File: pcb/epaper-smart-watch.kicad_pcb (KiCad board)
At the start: 2 copper layers, 29.2 x 29.2 mm, 66 parts, among them J1 AXT624124, J3 Lithium Battery 3.7V, M1 Motor_DC, P1 USB_C_Plug_USB2.0, Q1 MMBT3904, Q3 Si1308EDL, SW1 BTN, SW2 BTN, SW3 BTN, SW4 BTN, U1 CH340E, U2 STM32WB1MMCH6TR, U3 LSM6DS3

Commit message: V2 soon...
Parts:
- removed the C20 at (154.6, 100.1)
- removed the C21 at (156.5, 100.1)
- removed the C9 at (147.3, 94.3)
- removed the D1 at (138.0, 93.8)
- removed the D3 at (138.0, 96.7)
- removed the D4 at (138.0, 99.6)
- removed JP3: SolderJumper_3_Bridged12, Jumper:SolderJumper-3_P1.3mm_Bridged12_RoundedPad1.0x1.5mm_NumberLabels
- removed PS1: STNS01PUR, SamacSys:SON45P300X300X80-13N-D
- removed Q1: MMBT3904, Package_TO_SOT_SMD:SOT-23
- removed the R2 at (147.4, 98.3)
- removed the R9 at (136.8, 105.6)
- added AC1: BMA400, Package_LGA:LGA-12_2x2mm_P0.5mm, F.Cu at (225.1, 99.8)
- added BZ1: Buzzer, Jumper:SolderJumper-2_P1.3mm_Open_Pad1.0x1.5mm, B.Cu at (141.9, 107.2)
- added C10: 0.1uF, Capacitor_SMD:C_0402_1005Metric, F.Cu at (212.6, 103.7)
- added C22: 10uF, Capacitor_SMD:C_0603_1608Metric, F.Cu at (194.9, 87.4)
- added C5: 100nF, Capacitor_SMD:C_0402_1005Metric, F.Cu at (213.2, 98.0)
- added C6: 100nF, Capacitor_SMD:C_0402_1005Metric, F.Cu at (213.3, 95.1)
- added D2: LED, LED_SMD:LED_0603_1608Metric, F.Cu at (210.9, 100.0)
- added D6: MBR0530, Diode_SMD:D_SOD-123, F.Cu at (198.2, 90.3)
- added IC2: NPM1100-QDAA-R7, SamasSys:QFN50P400X400X90-25N-D, F.Cu at (141.6, 75.1)
- added IC3: MAX17048G+T10, SamasSys:SON50P200X200X80-9N-D, F.Cu at (214.8, 101.5)
- added IC4: AP3032, SamasSys:SOT95P280X145-6N, F.Cu at (130.1, 84.0)
- added J10: ~, TestPoint:TestPoint_Pad_D1.0mm, B.Cu at (170.4, 85.0)
- added J11: ~, TestPoint:TestPoint_Pad_D1.0mm, B.Cu at (170.4, 88.1)
- added J12: ~, TestPoint:TestPoint_Pad_D1.0mm, B.Cu at (170.4, 91.2)
- added J13: ~, TestPoint:TestPoint_Pad_D1.0mm, B.Cu at (173.5, 85.0)
- added J14: ~, TestPoint:TestPoint_Pad_D1.0mm, B.Cu at (173.5, 88.1)
- added J15: ~, TestPoint:TestPoint_Pad_D1.0mm, B.Cu at (173.5, 91.2)
- added J16: Touch3, TestPoint:TestPoint_Pad_D1.0mm, B.Cu at (163.3, 86.5)
- added J17: Touch2, TestPoint:TestPoint_Pad_D1.0mm, B.Cu at (163.3, 89.6)
- added J18: Touch1, TestPoint:TestPoint_Pad_D1.0mm, B.Cu at (163.3, 92.7)
- added J4: ~, TestPoint:TestPoint_Pad_D1.0mm, B.Cu at (162.7, 82.5)
- added J7: ~, TestPoint:TestPoint_Pad_D1.0mm, B.Cu at (167.4, 85.0)
- added J8: ~, TestPoint:TestPoint_Pad_D1.0mm, B.Cu at (167.4, 88.1)
- added J9: ~, TestPoint:TestPoint_Pad_D1.0mm, B.Cu at (167.4, 91.2)
- added L1: 2.2uH, Inductor_SMD:L_0603_1608Metric, F.Cu at (202.5, 99.6)
- added L3: 6.8uH, Inductor_SMD:L_0603_1608Metric, F.Cu at (200.2, 87.6)
- added Q3: AO3400A, Package_TO_SOT_SMD:SOT-23, F.Cu at (224.7, 95.8)
- added R1: 10k, Resistor_SMD:R_0402_1005Metric, F.Cu at (212.2, 96.7)
- added R1: 10k, Resistor_SMD:R_0402_1005Metric, F.Cu at (210.0, 91.5)
- added R10: 750k, Resistor_SMD:R_0402_1005Metric, F.Cu at (199.9, 82.4)
- added R11: 100k, Resistor_SMD:R_0402_1005Metric, F.Cu at (198.2, 84.3)
- added R13: 1k, Resistor_SMD:R_0402_1005Metric, F.Cu at (212.9, 101.1)
- added R2: 10k, Resistor_SMD:R_0402_1005Metric, F.Cu at (208.6, 93.7)
- added R2: 10k, Resistor_SMD:R_0402_1005Metric, F.Cu at (209.6, 93.7)
- added R5: 8.2k, Resistor_SMD:R_0402_1005Metric, F.Cu at (210.7, 97.0)
- added R8: 100k, Resistor_SMD:R_0402_1005Metric, F.Cu at (214.6, 93.0)
- added SW6: SW_Push, Button_Switch_SMD:SW_SPST_TS-1088-xR020, F.Cu at (158.4, 74.5)
- added U4: XT25F32FDTIGT, ProjectLibrary:DFN-8_L3.0-W2.0-P0.50-BL-EP_XT25XXX, F.Cu at (148.2, 75.1)
- C11: renamed from C13; value 2.2uF -> 100nF
- C13: renamed from C1; footprint Capacitor_SMD:C_0402_1005Metric -> Capacitor_SMD:C_0603_1608Metric
- C16: value 4.7uF -> 1uF; footprint Capacitor_SMD:C_0402_1005Metric -> Capacitor_SMD:C_0603_1608Metric
- C19: value 2.7pF -> 1uF/16V
- C2: renamed from C17; value 0.1uF -> 10uF; footprint Capacitor_SMD:C_0402_1005Metric -> Capacitor_SMD:C_0603_1608Metric
- C21: renamed from C4; footprint Capacitor_SMD:C_0402_1005Metric -> Capacitor_SMD:C_0603_1608Metric
- C22: value 2.2uF -> 3.3pF
- C24, C25: value 0.1uF -> 100nF
- C3: renamed from C18; footprint Capacitor_SMD:C_0402_1005Metric -> Capacitor_SMD:C_0603_1608Metric
- C4: renamed from C15; value 0.1uF -> 10uF; footprint Capacitor_SMD:C_0402_1005Metric -> Capacitor_SMD:C_0603_1608Metric
- C7: renamed from C14; value 1uF -> 2.2uF
- C8: renamed from C12; value 4.7uF -> 1uF
- J5: renamed from J3; moved to B.Cu
- J6: renamed from J1; footprint FPC:AXT624124 -> ProjectLibrary:AXT624124
- M1: moved to B.Cu
- P1: footprint USBC:USB-C-SMD_KH-TYPE-C-16P -> ProjectLibrary:USB-C-SMD_TYPE-C-16P-CB0.8-073
- Q2: renamed from Q3; footprint Package_TO_SOT_SMD:SOT-323_SC-70 -> Package_TO_SOT_SMD:SOT-23
- R12: renamed from R1; value 2k -> 100k
- R14: value 1k -> 100k
- R15: value 1k -> 10
- R16: value 1k -> 10k
- R6: renamed from R5; value 600 -> 1k
- R7: value 10K -> 100
- U1: value CH340E -> BME280; footprint Package_SO:MSOP-10_3x3mm_P0.5mm -> Package_LGA:Bosch_LGA-8_2.5x2.5mm_P0.65mm_ClockwisePinNumbering
- U2: value STM32WB1MMCH6TR -> USBLC6-2SC6; footprint EasyEda2Kicad:LGA-77_L10.0-W6.5-STM32WB1MMCH6TR -> Package_TO_SOT_SMD:SOT-23-6
- U3: value LSM6DS3 -> STM32WB5MMG; footprint Package_LGA:LGA-14_3x2.5mm_P0.5mm_LayoutBorder3x4y -> RF_Module:ST-SiP-LGA-86-11x7.3mm
- moved D3 73.3 mm to (210.9, 98.5), turned to 180 degrees
- moved C9 73.0 mm to (218.5, 89.0)
- moved U1 72.8 mm to (213.5, 91.1)
- moved D4 72.1 mm to (216.6, 91.2), turned to 90 degrees
- moved R3 71.6 mm to (207.5, 101.7)
- moved R16 71.6 mm to (215.5, 98.7), turned to 90 degrees
- moved D1 69.3 mm to (210.9, 101.5), turned to 0 degrees
- moved R14 69.0 mm to (211.0, 84.4)
- moved C2 68.6 mm to (207.7, 99.7)
- moved C22 68.0 mm to (209.6, 80.7), turned to 90 degrees
- moved C11 67.9 mm to (210.7, 95.8), turned to 180 degrees
- moved C8 67.8 mm to (208.9, 91.6), turned to 90 degrees
- moved C25 67.6 mm to (209.8, 84.7), turned to 90 degrees
- moved C4 67.5 mm to (208.9, 96.2)
- moved C24 67.2 mm to (209.7, 88.8)
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- renumbered C2 to C12, C8 to C14, C3 to C15, C11 to C17, C7 to C18, C6 to C19, C5 to C20, C10 to C23, C23 to C9, D6 to D1, D2 to D3, D9 to D4, D7 to D5, D5 to D7, L1 to L2, R6 to R9, SW1 to SW2, SW2 to SW3, SW3 to SW4, SW4 to SW5
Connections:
- net /RESR renamed /EPD_RESR
- net /VCOM renamed /EPD_VCOM
- net /VGH renamed /EPD_VGH
- net /VGL renamed /EPD_VGL
- C11 pad 1: /VBUS -> +3V0
- C12 pad 1: /EPD_VDD -> +3V0
- C13 pad 1: /EPD_VDD -> +3V0
- C16 pad 1: /EPD_VDD -> /EPD_LIGHT_PWR_POS
- C16 pad 2: GND -> /EPD_LIGHT_PWR_NEG
- C19 pad 1: Net-(U2-PB1) -> Net-(J6-Pin_5)
- C19 pad 1: Net-(J1-Pin_5) -> Net-(J6-Pin_5)
- C2 pad 1: Net-(U1-V3) -> +3V0
- C24 pad 1: /EPD_VDD -> GND
- C24 pad 2: GND -> /NRST
- C25 pad 1: /EPD_VDD -> GND
- C25 pad 2: GND -> Net-(U3-PC13)
- C3 pad 1: Net-(U1-~{RTS}) -> Net-(IC2-DEC)
- C3 pad 2: /NRST -> GND
- C4 pad 1: /VBUS -> /VSYS
- C7 pad 1: /EPD_VDD -> +5V
- C9 pad 1: Net-(D9-K) -> +3V0
- C9 pad 2: GND -> Net-(D4-A)
- D1 pad 1: GND -> Net-(D1-K)
- D1 pad 2: Net-(D6-A) -> /VSYS
- D3 pad 1: /CHG -> GND
- D4 pad 1: Net-(D9-K) -> +3V0
- D4 pad 2: GND -> Net-(D4-A)
- J5 pad 2: GND -> Net-(J5-Pin_2)
- J5 pad 3: Net-(J3-Pin_3) -> GND
- J6 pad 12: /CSB -> /EPD_CSB
- J6 pad 13: /DC -> /EPD_DC
- J6 pad 14: /RST_N -> /EPD_RST_N
- J6 pad 15: /BUSY -> /EPD_BUSY
- J6 pad 16: Net-(J1-Pin_16) -> Net-(J6-Pin_16)
- J6 pad 21: /GDR -> /EPD_GDR
- J6 pad 23: /FL+ -> /EPD_LIGHT_PWR_POS
- J6 pad 24: /FL- -> /EPD_LIGHT_PWR_NEG
- J6 pad 5: Net-(J1-Pin_5) -> Net-(J6-Pin_5)
- J6 pad 9: /EPD_VDD -> +3V0
- JP1 pad 1: Net-(JP1-A) -> Net-(J6-Pin_16)
- JP1 pad 2: /TXD -> GND
- JP1 pad 3: Net-(JP1-B) -> +3V0
- JP2 pad 1: Net-(JP1-B) -> Net-(JP2-A)
- JP2 pad 2: /RXD -> Net-(IC2-NTC)
- JP2 pad 3: Net-(JP1-A) -> Net-(J5-Pin_2)
- L2 pad 1: /EPD_VDD -> +3V0
- M1 pad 1: Net-(D9-K) -> +3V0
- M1 pad 2: GND -> Net-(D4-A)
- P1 pad A6: /D+ -> Net-(P1-D+-PadA6)
- P1 pad A7: /D- -> Net-(P1-D--PadA7)
- P1 pad A8: unconnected-(P1-SBU1-PadA8) -> (no net)
- P1 pad B6: /D+ -> Net-(P1-D+-PadA6)
- P1 pad B7: /D- -> Net-(P1-D--PadA7)
- P1 pad B8: unconnected-(P1-SBU2-PadB8) -> (no net)
- Q2 pad 1: /GDR -> /EPD_GDR
- R12 pad 1: Net-(PS1-ISET) -> GND
- R12 pad 2: Net-(R1-Pad2) -> /EPD_GDR
- R14 pad 1: Net-(U1-TNOW) -> +3V0
- R14 pad 2: Net-(D6-A) -> /FLASH_CS
- R15 pad 1: Net-(U1-TXD) -> GND
- R15 pad 2: Net-(JP1-A) -> /EPD_LIGHT_PWR_NEG
- R16 pad 1: Net-(U1-RXD) -> Net-(JP2-A)
- R16 pad 2: Net-(JP1-B) -> GND
- R6 pad 1: /EPD_VDD -> +5V
- R7 pad 1: /EPD_VDD -> Net-(Q3-G)
- R7 pad 2: /Accel_SDA -> /VIB
- SWD1 pad 6: /EPD_VDD -> +3V0
- U1 pad 1: /D+ -> GND
- U1 pad 2: /D- -> Net-(U1-CSB)
- U1 pad 3: GND -> /ACCL_SDA
- U1 pad 4: Net-(U1-~{RTS}) -> /ACCL_SCL
- U1 pad 5: unconnected-(U1-~{CTS}-Pad5) -> GND
- U1 pad 6: Net-(U1-TNOW) -> +3V0
- U1 pad 7: /VBUS -> GND
- U1 pad 8: Net-(U1-TXD) -> +3V0
- U2 pad 1: GND -> Net-(P1-D--PadA7)
- U2 pad 3: GND -> Net-(P1-D+-PadA6)
- U2 pad 4: GND -> /D+
- U2 pad 5: GND -> +5V
- U2 pad 6: Net-(U2-ANT_IN) -> /D-
- U3 pad 1: unconnected-(U3-SDO/SA0-Pad1) -> /EPD_BUSY
- U3 pad 10: unconnected-(U3-NC-Pad10) -> /NRST
- U3 pad 11: unconnected-(U3-NC-Pad11) -> /ACCL_SDA
- U3 pad 12: /Accel_CS -> /ACCL_INT1
- U3 pad 13: /Accel_SCL -> Net-(U3-PH3-BOOT0)
- U3 pad 14: /Accel_SDA -> /ACCL_SCL
- U3 pad 4: /Accel_INT1 -> +3V0
- U3 pad 5: /EPD_VDD -> GND
- U3 pad 6: GND -> +3V0
- U3 pad 7: GND -> unconnected-(U3-PC3-Pad7)
- U3 pad 8: /EPD_VDD -> unconnected-(U3-PC2-Pad8)
- U3 pad 9: unconnected-(U3-INT2-Pad9) -> /ACCL_INT2
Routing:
- net /EPD_VDD: track 71.7 -> 0.00 mm, vias 8 -> 0
- net GND: track 54.7 -> 0.00 mm, vias 17 -> 0
- net /VBUS: track 34.2 -> 0.00 mm, vias 5 -> 0
- net /BTN_1: track 32.7 -> 0.00 mm, vias 2 -> 0
- net /BTN_4: track 24.7 -> 0.00 mm, vias 2 -> 0
- net /RST_N: track 22.1 -> 0.00 mm, vias 2 -> 0
- net /BUSY: track 18.6 -> 0.00 mm, vias 2 -> 0
- net /DC: track 18.4 -> 0.00 mm, vias 2 -> 0
- net /BATMS: track 18.3 -> 0.00 mm, vias 2 -> 0
- net /EPD_SPICL: track 18.1 -> 0.00 mm, vias 2 -> 0
- net /EPD_MOSI: track 17.0 -> 0.00 mm, vias 2 -> 0
- net /CSB: track 15.1 -> 0.00 mm, vias 2 -> 0
- net Net-(D5-A): track 15.0 -> 0.00 mm
- net /NRST: track 14.9 -> 0.00 mm, vias 3 -> 0
- net /RXD: track 11.7 -> 0.00 mm, vias 1 -> 0
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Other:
- board size 29.2 x 29.2 mm -> 41 x 36 mm
- copper layers 2 -> 4

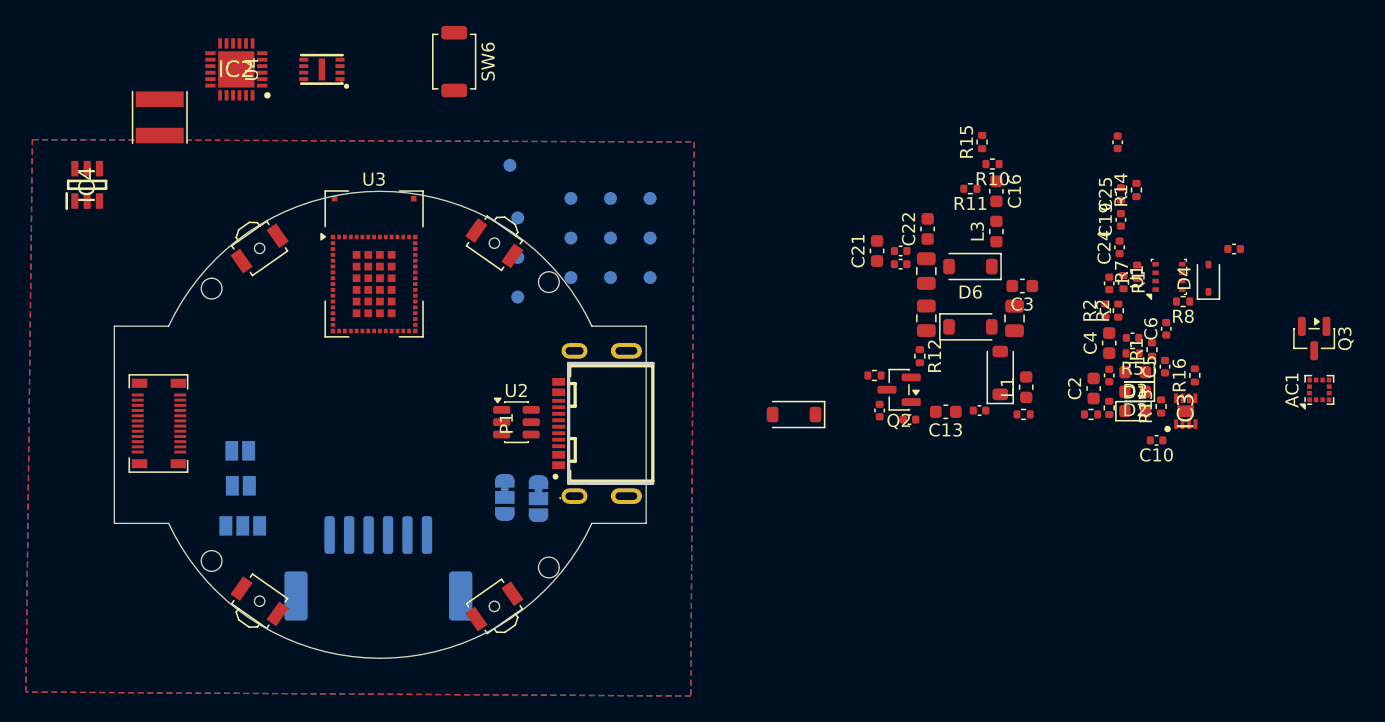
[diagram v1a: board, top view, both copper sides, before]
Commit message: Routed the board, will do verification check soon
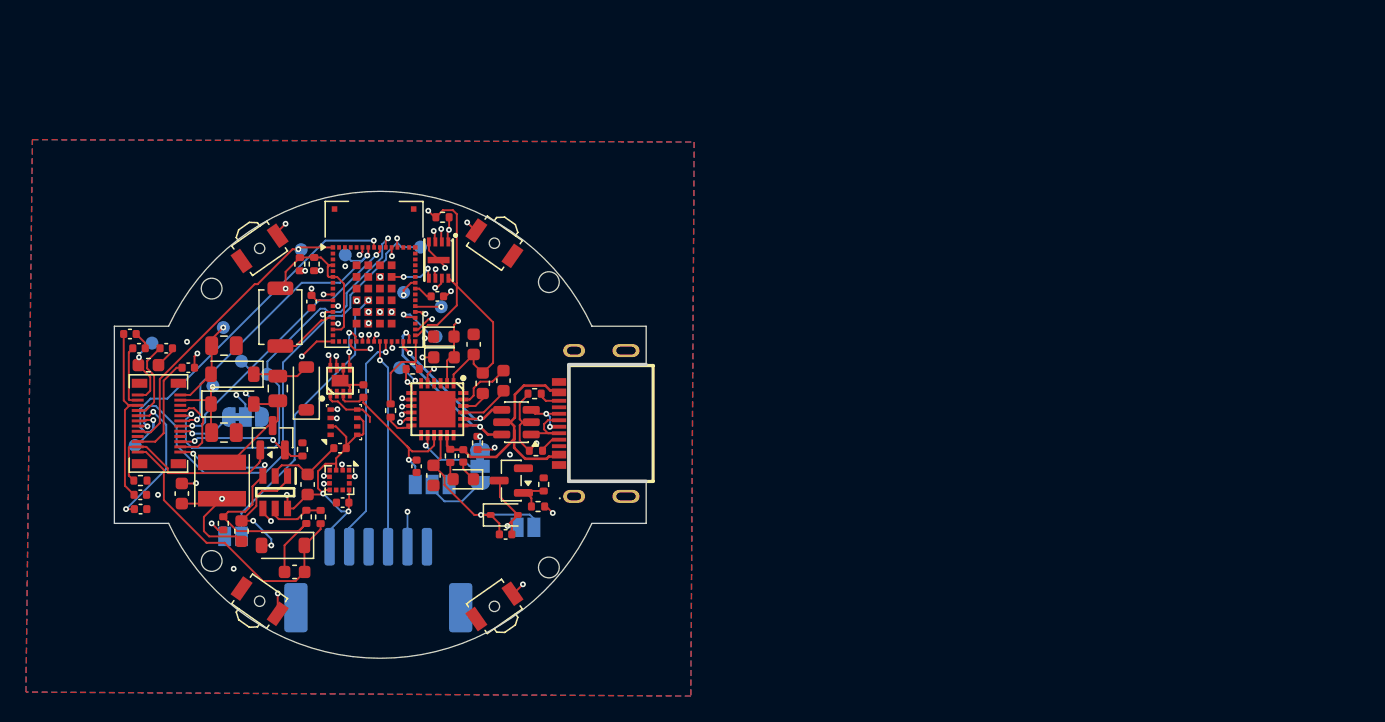
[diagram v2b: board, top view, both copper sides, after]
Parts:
- removed the C22 at (209.6, 80.7)
- removed C5: 100nF, Capacitor_SMD:C_0402_1005Metric
- removed the R1 at (212.2, 96.7)
- removed the R1 at (210.0, 91.5)
- removed the R2 at (208.6, 93.7)
- removed the R2 at (209.6, 93.7)
- added R1: 10k, Resistor_SMD:R_0402_1005Metric, F.Cu at (147.6, 90.1)
- added R2: 10k, Resistor_SMD:R_0402_1005Metric, F.Cu at (146.5, 90.1)
- P1: footprint ProjectLibrary:USB-C-SMD_TYPE-C-16P-CB0.8-073 -> USB-C-SMD_SHOU_TYPE-C-16P-CB1.6
- moved C19 78.5 mm to (134.2, 107.9), turned to 0 degrees
- moved AC1 75.9 mm to (149.6, 106.8), turned to -90 degrees
- moved R15 65.5 mm to (140.6, 110.1)
- moved IC3 65.2 mm to (149.6, 99.1)
- moved C12 65.1 mm to (134.2, 109.0)
- moved U1 64.6 mm to (149.9, 102.3)
- moved C6 64.4 mm to (149.6, 104.3), turned to 0 degrees
- moved Q3 62.9 mm to (162.8, 106.8), turned to 180 degrees
- moved L3 62.6 mm to (142.0, 110.7), turned to -90 degrees
- moved C24 62.4 mm to (147.4, 93.0)
- moved C11 62.2 mm to (149.8, 108.5)
- moved C16 61.6 mm to (146.1, 113.8), turned to 180 degrees
- moved C10 61.3 mm to (151.4, 99.9), turned to 90 degrees
- moved R12 60.9 mm to (134.2, 106.8), turned to 180 degrees
- moved C9 60.3 mm to (162.4, 111.0)
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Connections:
- C9 pad 1: +3V0 -> /VSYS
- D4 pad 1: +3V0 -> /VSYS
- M1 pad 1: +3V0 -> /VSYS
- U1 pad 2: Net-(U1-CSB) -> +3V0
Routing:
- net +3V0: track 0.00 -> 143.6 mm, vias 0 -> 10
- net GND: track 0.00 -> 74.0 mm, vias 0 -> 14
- net /VSYS: track 0.00 -> 41.5 mm, vias 0 -> 3
- net /EPD_DC: track 0.00 -> 40.0 mm, vias 0 -> 2
- net /EPD_MOSI: track 0.00 -> 32.8 mm, vias 0 -> 2
- net /EPD_SPICL: track 0.00 -> 32.4 mm, vias 0 -> 2
- net /BTN_4: track 0.00 -> 26.3 mm, vias 0 -> 2
- net /BTN_1: track 0.00 -> 24.9 mm, vias 0 -> 2
- net /EPD_LIGHT_PWR_NEG: track 0.00 -> 24.8 mm, vias 0 -> 2
- net /NRST: track 0.00 -> 24.7 mm, vias 0 -> 2
- net /EPD_CSB: track 0.00 -> 23.9 mm, vias 0 -> 2
- net /EPD_LIGHT: track 0.00 -> 23.6 mm, vias 0 -> 2
- net /EPD_BUSY: track 0.00 -> 23.0 mm, vias 0 -> 1
- net /EPD_LIGHT_PWR_POS: track 0.00 -> 22.9 mm
- net /VIB: track 0.00 -> 22.7 mm, vias 0 -> 2
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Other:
- outline, holes or cut-outs redrawn

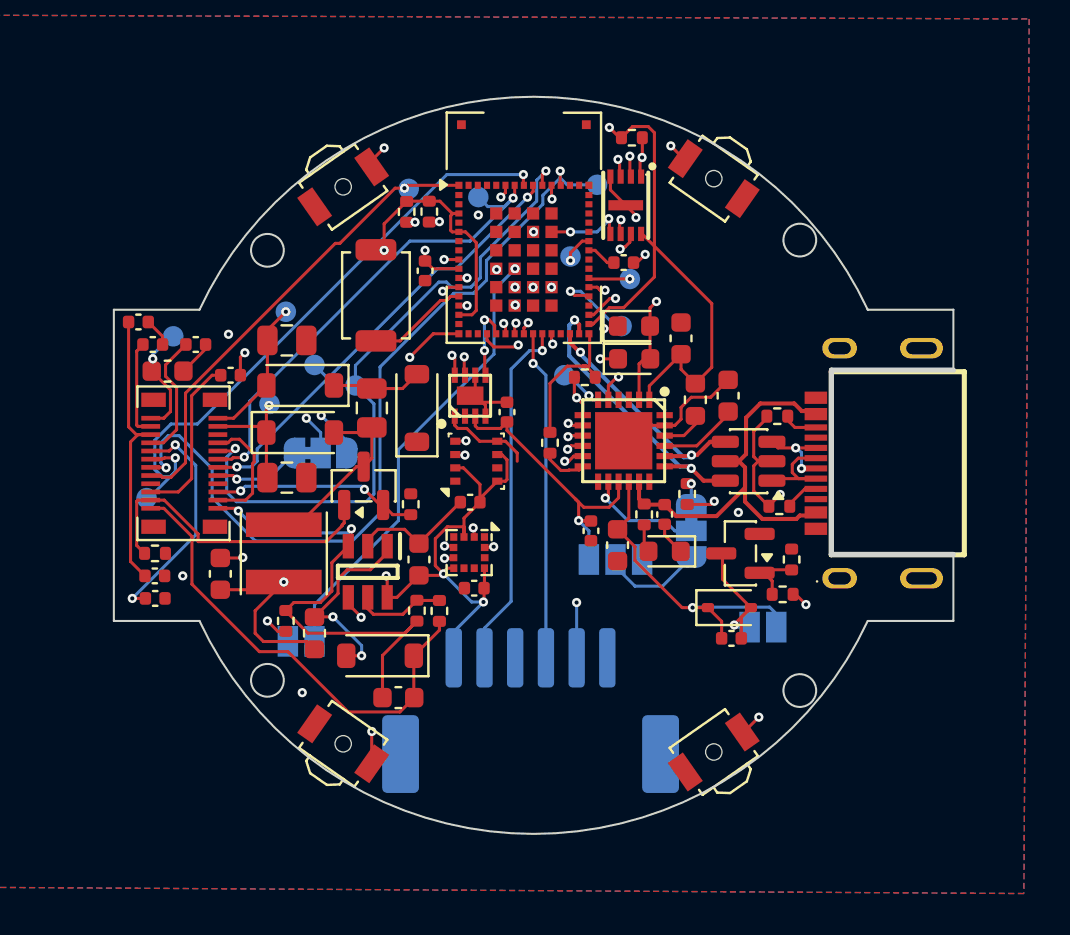
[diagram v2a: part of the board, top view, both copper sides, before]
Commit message: Routed board
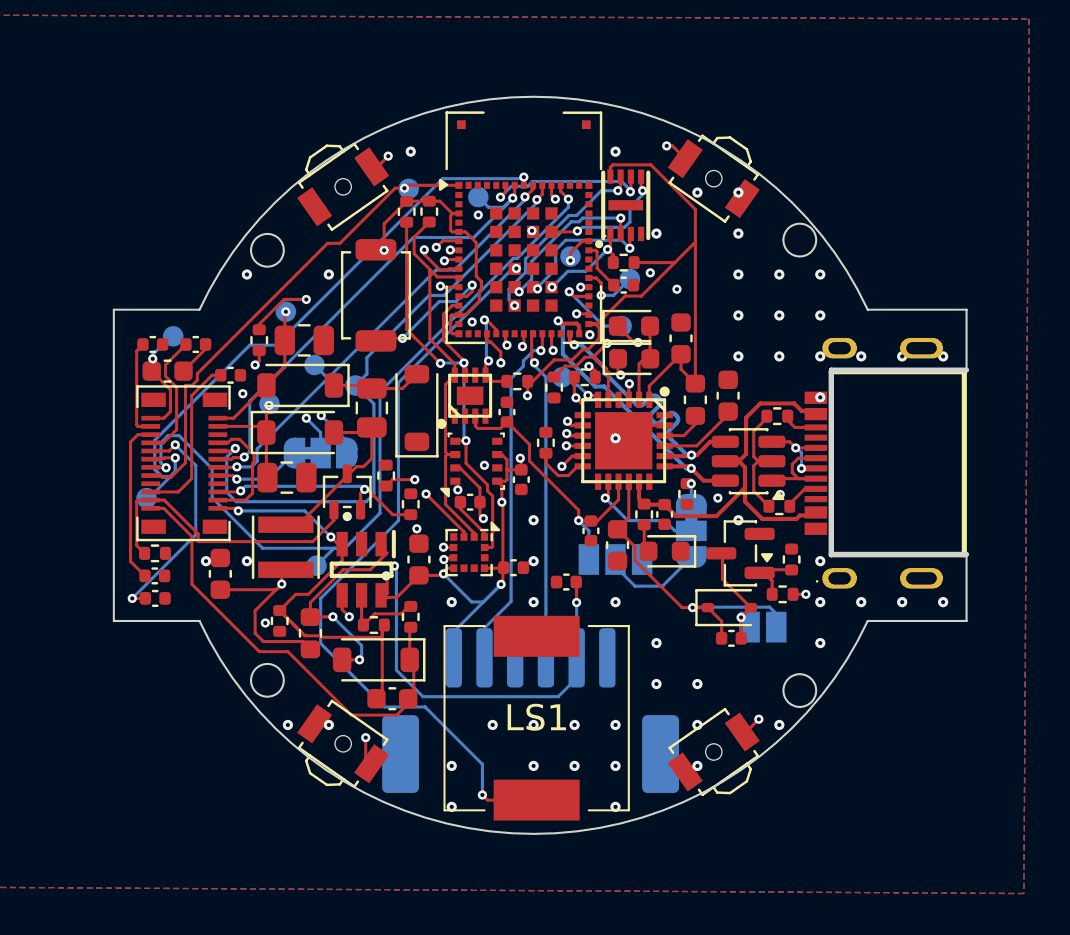
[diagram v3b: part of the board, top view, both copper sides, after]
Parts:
- removed BZ1: Buzzer, Jumper:SolderJumper-2_P1.3mm_Open_Pad1.0x1.5mm
- removed the C19 at (133.4, 95.5)
- added C26: 100nF, Capacitor_SMD:C_0402_1005Metric, F.Cu at (152.1, 103.2)
- added LS1: CPT-9019S-SMT-TR, SamasSys:CPT9019SSMTTR, F.Cu at (152.8, 114.8)
- added R17: 10k, Resistor_SMD:R_0402_1005Metric, F.Cu at (151.9, 98.4)
- added R18: 10k, Resistor_SMD:R_0402_1005Metric, F.Cu at (153.7, 98.7)
- added R19: 10k, Resistor_SMD:R_0402_1005Metric, F.Cu at (139.3, 96.4)
- added R20: 100k, Resistor_SMD:R_0402_1005Metric, F.Cu at (145.5, 103.0)
- L2: footprint Inductor_SMD:L_Taiyo-Yuden_NR-40xx -> Inductor_SMD:L_Taiyo-Yuden_NR-30xx
- P1: footprint USB-C-SMD_SHOU_TYPE-C-16P-CB1.6 -> ProjectLibrary:USB-C-SMD_SHOU_TYPE-C-16P-CB1.6
- Q2: footprint Package_TO_SOT_SMD:SOT-23 -> Package_TO_SOT_SMD:SOT-323_SC-70
- R5: value 8.2k -> 22k
- moved J13 23.1 mm to (142.1, 107.4)
- moved C24 16.7 mm to (154.3, 108.2), turned to 0 degrees
- moved R14 6.11 mm to (157.1, 92.6), turned to 180 degrees
- moved R11 2.21 mm to (144.9, 110.3), turned to 0 degrees
- moved C11 2.16 mm to (151.7, 107.5), turned to 0 degrees
- moved R10 1.43 mm to (146.7, 109.9)
- moved C25 1.10 mm to (157.1, 93.7)
- moved Q2 0.85 mm to (143.6, 103.8)
- moved C23 0.85 mm to (141.5, 96.4)
- moved L2 0.32 mm to (140.6, 106.5)
- moved IC4 0.32 mm to (144.3, 107.6)
- moved C16 0.30 mm to (145.8, 113.9)
- moved R15 0.30 mm to (140.3, 110.1)
- moved D6 0.28 mm to (145.0, 112.0)
- moved L3 0.20 mm to (141.8, 110.7)
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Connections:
- net /ACCL_SCL renamed /I2C_SCL
- net /ACCL_SDA renamed /I2C_SDA
- IC2 pad 4: unconnected-(IC2-NC_1-Pad4) -> GND
- U3 pad 23: /BTN_2 -> unconnected-(U3-PC11-Pad23)
- U3 pad 64: /EPD_LIGHT -> unconnected-(U3-PE1-Pad64)
- U3 pad 7: unconnected-(U3-PC3-Pad7) -> /EPD_LIGHT
- U3 pad 8: unconnected-(U3-PC2-Pad8) -> /BTN_2
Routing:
- net GND: track 74.0 -> 19.2 mm, vias 14 -> 70
- net /SND: track 22.3 -> 37.0 mm, vias 1 -> 2
- net /NRST: track 24.7 -> 36.8 mm, vias 2 -> 3
- net /BTN_2: track 13.7 -> 7.12 mm
- net Net-(J6-Pin_5): track 14.3 -> 7.97 mm
- net /FLASH_CLK: track 14.0 -> 8.35 mm
- net /EPD_CSB: track 23.9 -> 29.5 mm, vias 2 -> 3
- net /FLASH_CS: track 10.2 -> 5.05 mm
- net /VSYS: track 41.5 -> 37.5 mm
- net /BTN_1: track 24.9 -> 28.6 mm
- net /FLASH_IO1: track 10.9 -> 7.74 mm
- net /D+: track 12.3 -> 15.2 mm
- net /BTN_3: track 14.0 -> 16.8 mm
- net /EPD_MOSI: track 32.8 -> 30.4 mm
- net /FLASH_IO0: track 4.31 -> 6.53 mm
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- added copper zone on In1.Cu, net GND
- added copper zone on In2.Cu, net GND
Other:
- board size 41 x 36 mm -> 41.6 x 36 mm

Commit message: Final production V2 ready
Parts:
- removed D4: D, Diode_SMD:D_SOD-323
- added C27: 1uF/16V, Capacitor_SMD:C_0402_1005Metric, F.Cu at (161.4, 96.4)
- added C5: 1uF/16V, Capacitor_SMD:C_0402_1005Metric, F.Cu at (165.8, 96.3)
- added D9: MBR0530, Diode_SMD:D_SOD-123, F.Cu at (163.7, 110.7)
- added Q4: AO3400A, Package_TO_SOT_SMD:SOT-23, F.Cu at (160.3, 112.4)
- added R21: 1k, Resistor_SMD:R_0402_1005Metric, F.Cu at (145.4, 90.7)
- added R22: 100, Resistor_SMD:R_0402_1005Metric, F.Cu at (158.9, 114.9)
- added R23: 100k, Resistor_SMD:R_0402_1005Metric, F.Cu at (163.2, 112.4)
- added R24: 1k, Resistor_SMD:R_0402_1005Metric, F.Cu at (160.2, 110.2)
- added U5: XC6206P332MR, Package_TO_SOT_SMD:SOT-23-3, F.Cu at (163.6, 96.4)
- C14: footprint Capacitor_SMD:C_0402_1005Metric -> Capacitor_SMD:C_0603_1608Metric
- C16: value 1uF -> 1uF/16V
- C19, C20: value 1uF/16V -> 1uF/25V; footprint Capacitor_SMD:C_0402_1005Metric -> Capacitor_SMD:C_0603_1608Metric
- C7: value 2.2uF -> 2.2uF/25V; footprint Capacitor_SMD:C_0402_1005Metric -> Capacitor_SMD:C_0805_2012Metric
- C9: value 0.1uF/6.3V -> 0.1uF/16V
- R15: value 10 -> 100
- moved J18 6.44 mm to (159.2, 96.7)
- moved L3 6.22 mm to (146.8, 107.0)
- moved C22 5.95 mm to (141.8, 109.8), turned to -90 degrees
- moved C8 2.89 mm to (153.5, 103.6), turned to 180 degrees
- moved C9 2.17 mm to (161.4, 109.0)
- moved D3 1.90 mm to (157.2, 106.7), turned to 0 degrees
- moved C7 1.88 mm to (159.8, 106.7)
- moved J16 1.84 mm to (158.8, 94.6)
- moved C4 1.38 mm to (156.1, 105.2), turned to 180 degrees
- moved R15 1.35 mm to (139.2, 109.3), turned to 0 degrees
- moved C14 0.91 mm to (138.0, 97.2), turned to 90 degrees
- moved C20 0.73 mm to (134.8, 96.4)
- moved C18 0.72 mm to (136.8, 97.0), turned to 90 degrees
- moved R2 0.31 mm to (146.8, 90.2)
- moved C12 0.27 mm to (134.4, 109.2)
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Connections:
- C22 pad 1: +3V0 -> /VSYS
- C25 pad 1: GND -> Net-(U3-PB12)
- C25 pad 2: Net-(U3-PC13) -> GND
- IC4 pad 6: +3V0 -> /VSYS
- JP1 pad 1: Net-(J6-Pin_16) -> GND
- JP1 pad 2: GND -> Net-(J6-Pin_16)
- L3 pad 2: +3V0 -> /VSYS
- LS1 pad 1: GND -> Net-(Q4-D)
- LS1 pad 2: /SND -> /VSYS
- SW6 pad 1: +3V0 -> Net-(R21-Pad2)
- U3 pad 32: +3V0 -> /VUSB
- U3 pad 35: Net-(J17-Pin_1) -> Net-(J18-Pin_1)
- U3 pad 37: Net-(J16-Pin_1) -> Net-(J17-Pin_1)
- U3 pad 38: unconnected-(U3-PB15-Pad38) -> Net-(J16-Pin_1)
- U3 pad 40: Net-(U3-PC13) -> unconnected-(U3-PC13-Pad40)
- U3 pad 41: Net-(J18-Pin_1) -> Net-(U3-PB12)
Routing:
- net /VSYS: track 37.5 -> 67.6 mm, vias 3 -> 6
- net /VUSB: track 0.00 -> 10.4 mm, vias 0 -> 2
- net Net-(Q4-D): track 0.00 -> 9.95 mm
- net +3V0: track 143.0 -> 134.6 mm
- net Net-(Q4-G): track 0.00 -> 7.50 mm
- net /SND: track 37.0 -> 42.7 mm
- net +5V: track 20.3 -> 24.9 mm
- net Net-(D9-A): track 5.54 -> 9.98 mm
- net GND: track 19.2 -> 15.6 mm, vias 70 -> 60
- net Net-(J18-Pin_1): track 1.51 -> 4.94 mm
- net /EPD_SPICL: track 33.1 -> 29.8 mm
- net Net-(U3-PB12): track 0.00 -> 2.79 mm
- net Net-(U3-PC13): track 2.40 -> 0.00 mm
- net Net-(J6-Pin_5): track 7.97 -> 10.2 mm, vias 0 -> 2
- net Net-(IC2-NTC): track 5.72 -> 7.90 mm
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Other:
- board text added: "JLCJLCJLCJLC"
